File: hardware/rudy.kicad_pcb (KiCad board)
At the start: 2 copper layers, 15.7 x 67.1 mm, 23 parts, among them IC1 ATMEGA328-P, P1 CONN1, P2 CONN2, P3 SERPROG, P4 USB_B, U1 LD1117S33TR, Y1 Crystal

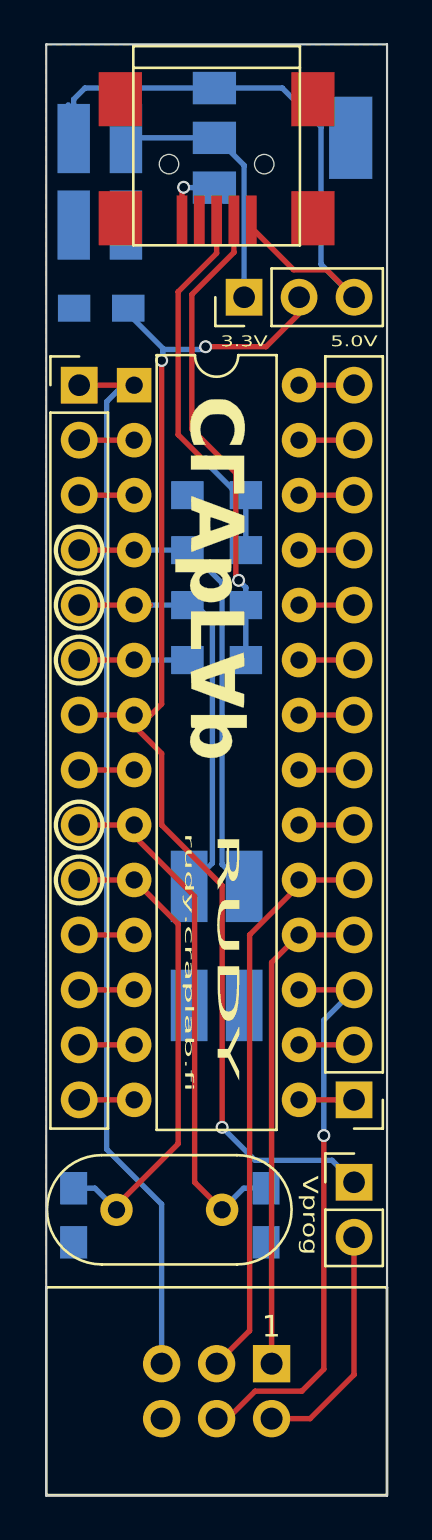
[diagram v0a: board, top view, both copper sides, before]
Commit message: Hardware revision A adjustments
Second iteration, changing SMD footprints from hand solder types to
normal / reflow types. Re-arranging power selector and re-routing
everything, fixing some minor general things along the way.

Changed Zener diode / resistor order for USB D+/D- lines.

Added solder paste layer Gerber file.
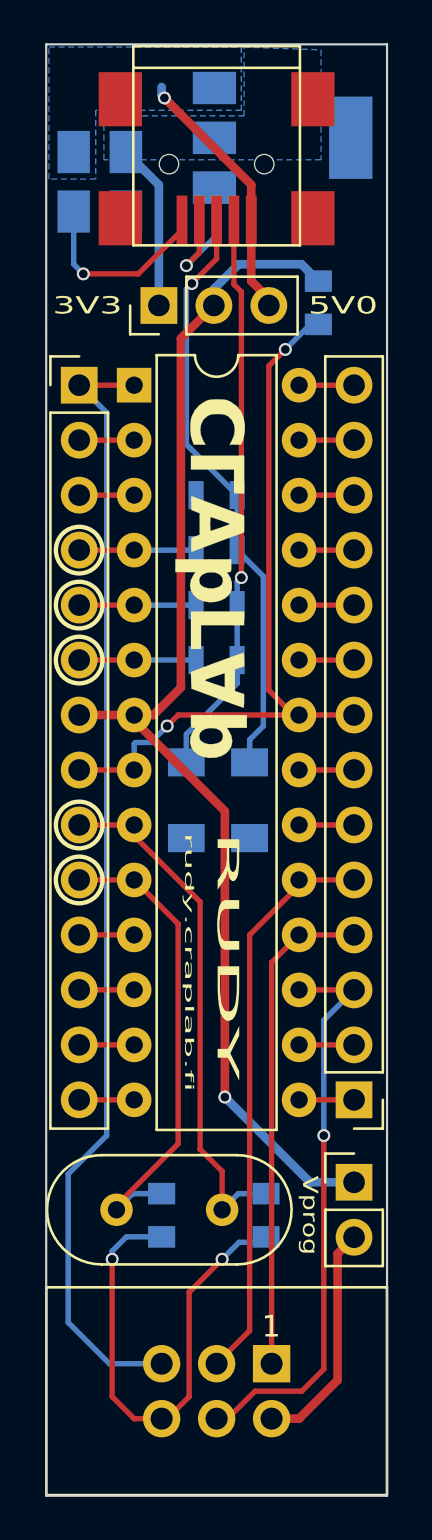
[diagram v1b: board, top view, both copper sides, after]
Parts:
- removed G2: LOGO, Artwork_4chord-midi:craplab-yknot-silk
- added G***: LOGO, Artwork_4chord-midi:craplab-2400, B.Cu at (76.2, 71.5)
- C1: footprint Capacitors_SMD:C_0805_HandSoldering -> Capacitors_SMD:C_0805
- C2, C3: footprint Capacitors_Tantalum_SMD:CP_Tantalum_Case-A_EIA-3216-18_Hand -> Capacitors_Tantalum_SMD:CP_Tantalum_Case-A_EIA-3216-18_Reflow
- C4, C5: value C -> 22p; footprint Capacitors_SMD:C_0805_HandSoldering -> Capacitors_SMD:C_0805
- D1, D2: footprint Diodes_SMD:D_MiniMELF_Handsoldering -> Diodes_SMD:D_MiniMELF
- R1, R2, R3, R4: footprint Resistors_SMD:R_0805_HandSoldering -> Resistors_SMD:R_0805
- moved G*** 15.2 mm to (76.2, 97.8)
- moved C1 10.0 mm to (80.9, 67.3), turned to 270 degrees
- moved D2 6.74 mm to (77.7, 90.3)
- moved D1 6.73 mm to (74.8, 90.3)
- moved C5 4.06 mm to (73.7, 109.5)
- moved JP1 3.96 mm to (73.5, 67.4)
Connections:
- D1 pad 1: /PD3 -> Net-(D1-Pad1)
- D2 pad 1: /PD2 -> Net-(D2-Pad1)
- P4 pad 2: Net-(P4-Pad2) -> Net-(D1-Pad1)
- P4 pad 3: Net-(P4-Pad3) -> Net-(D2-Pad1)
- R1 pad 2: Net-(P4-Pad2) -> Net-(D1-Pad1)
- R2 pad 2: Net-(P4-Pad3) -> Net-(D2-Pad1)
- R3 pad 2: Net-(P4-Pad2) -> Net-(D1-Pad1)
- R4 pad 1: Net-(P4-Pad3) -> Net-(D2-Pad1)
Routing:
- net GND: track 8.15 -> 74.8 mm, vias 1 -> 6
- net Net-(D2-Pad1): track 0.00 -> 27.4 mm, vias 0 -> 1
- net Net-(D1-Pad1): track 0.00 -> 26.8 mm, vias 0 -> 1
- net Net-(P4-Pad2): track 22.7 -> 0.00 mm, vias 1 -> 0
- net Net-(C2-Pad1): track 33.1 -> 12.5 mm, vias 0 -> 1
- net Net-(P4-Pad3): track 17.5 -> 0.00 mm, vias 1 -> 0
- net /PD2: track 22.3 -> 5.40 mm
- net /PD3: track 19.9 -> 5.40 mm
- net Net-(C3-Pad1): track 12.1 -> 8.19 mm
- net /#RESET: track 49.6 -> 52.7 mm
- net /VCC: track 58.7 -> 58.2 mm, vias 3 -> 1
- added copper zone on B.Cu, net Net-(C2-Pad1)
- added copper zone on B.Cu, net Net-(C3-Pad1)
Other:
- net class Power added: clearance 0.2, trace_width 0.4, via_dia 0.6, via_drill 0.4
- board text added: "3V3"
- board text added: "5V0"
- board text added: "CERN OHL v.1.2"
- board text added: "Revision A 08-2017"
- board text removed: "3.3V"
- board text removed: "5.0V"
- board text removed: "Licensed under CERN OHL v1.2"
- board text removed: "Revision A 07-2017"
